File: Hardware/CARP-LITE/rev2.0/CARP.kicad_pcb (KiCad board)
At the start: 4 copper layers, 70.1 x 40 mm, 159 parts, among them J1 USB-C, J10 PYRO_2, J11 RF_L, J3 I2C1+3V3, J4 2/3S XT30, J5 UART+5V+I2C1, J6 PYRO_1, J7 SPI, J8 PWM1+5V1, J9 PWM2+5V1, Q5 SQ2318CES, Q6 SQ2318CES, Q7 SQ2318CES, SW1 SW_Push, SW2 SW_Push, U1 BQ25792, U10 TPS62130A, U2 W25Q128JVSIMTR (16MB), U3 BMP581, U4 RP2350_60QFN, U5 LSM6DSO, U7 TLV75733PDBV, U9 LR2021IMLTRT, Y1 ABM8-272-T3, Y2 ECS-TXO-25CSMV-320-AN-TR

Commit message: pcb and schematic changes
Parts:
- removed the REF** at (447.6, 301.7)
- moved J7 449.6 mm to (116.0, 77.0)
- moved L15 418.5 mm to (157.1, 81.3), turned to 90 degrees
- moved U1 374.6 mm to (160.8, 81.2), turned to 90 degrees
- moved C59 364.3 mm to (146.4, 64.5)
- moved L2 359.4 mm to (95.1, 82.3)
- moved FB1 358.2 mm to (99.1, 82.1)
- moved R37 357.1 mm to (152.3, 64.7)
- moved C26 351.6 mm to (161.7, 64.1)
- moved C61 350.5 mm to (155.0, 68.2)
- moved C58 349.9 mm to (151.7, 70.6)
- moved R36 349.7 mm to (154.4, 71.3)
- moved R23 349.7 mm to (156.8, 71.8)
- moved C35 348.5 mm to (144.3, 83.8)
- moved L8 348.3 mm to (110.9, 93.3)
- moved C1 348.3 mm to (120.8, 89.1)
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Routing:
- net +5V: track 95.3 -> 51.9 mm
- net /GPIO2: track 28.1 -> 13.4 mm
- net /GPIO3: track 27.5 -> 13.1 mm
- net /Radio/VR_PA: track 11.5 -> 0.00 mm, vias 2 -> 0
- net /GPIO8: track 16.8 -> 5.50 mm
- net /GPIO9: track 16.7 -> 5.96 mm
- net /Radio/RFI_LF: track 10.6 -> 0.00 mm
- net /GPIO20: track 31.3 -> 21.6 mm
- net /Radio/RFO_LF1: track 7.17 -> 0.00 mm
- net Net-(J11-In): track 7.16 -> 0.03 mm
- net Net-(U9-LXB): track 4.98 -> 0.00 mm
- net Net-(U10-FB): track 3.96 -> 0.00 mm
- net Net-(C46-Pad1): track 3.36 -> 0.01 mm
- net Net-(C48-Pad2): track 3.10 -> 0.10 mm
- net +3V3: track 26.9 -> 24.4 mm, vias 24 -> 21
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- removed copper zone on F.Cu, net +5V
- removed copper zone on F.Cu, net /BAT
- removed copper zone on F.Cu, net Net-(L14-Pad1)
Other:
- board text added: "SPI"
- board text removed: "L2"
- board text removed: "R23"

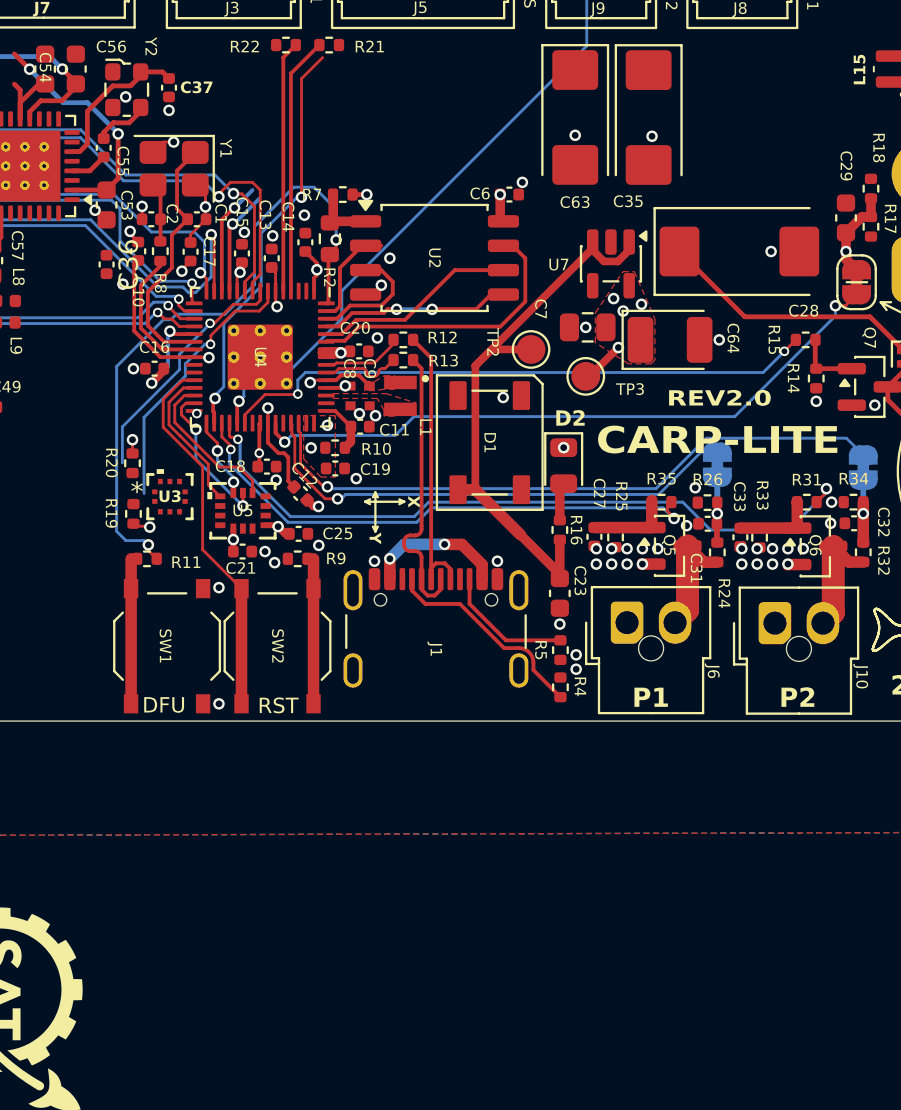
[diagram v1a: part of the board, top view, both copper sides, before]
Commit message: lithium charger is for carp lite rev 2, not carp dev
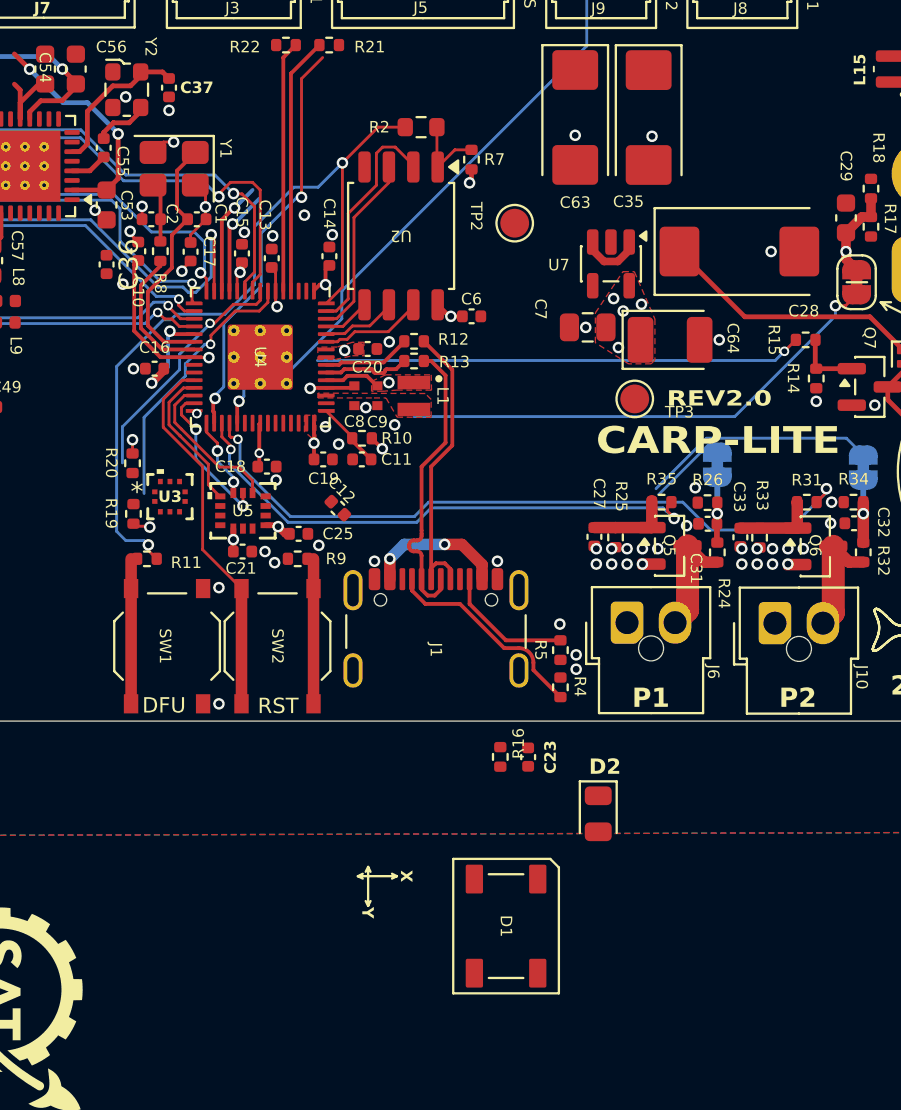
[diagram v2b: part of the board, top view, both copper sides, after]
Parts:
- C23: footprint Capacitor_SMD:C_0603_1608Metric -> Capacitor_SMD:C_0402_1005Metric
- moved D1 25.2 mm to (136.9, 125.9)
- moved D2 18.2 mm to (141.7, 120.0)
- moved R16 12.2 mm to (136.6, 117.1)
- moved C23 8.68 mm to (138.1, 117.1)
- moved R2 7.50 mm to (132.5, 84.3), turned to 0 degrees
- moved R7 6.94 mm to (135.1, 86.0), turned to 90 degrees
- moved C6 6.64 mm to (135.1, 94.2)
- moved TP2 6.63 mm to (137.3, 89.3)
- moved TP3 2.81 mm to (143.6, 98.5)
- moved C12 2.08 mm to (128.1, 104.1)
- moved U2 2.08 mm to (131.4, 90.0), turned to -90 degrees
- moved C11 1.71 mm to (129.4, 101.6), turned to 180 degrees
- moved R10 1.48 mm to (129.4, 100.5), turned to 180 degrees
- moved C14 1.45 mm to (127.7, 91.0)
- moved C19 0.79 mm to (127.4, 101.6)
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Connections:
- R18 pad 2: +2S -> /BAT
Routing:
- net +5V: track 51.9 -> 24.2 mm
- net Net-(U4-GPIO28_ADC2): track 26.1 -> 3.96 mm, vias 1 -> 0
- net Net-(U4-GPIO29_ADC3): track 33.4 -> 12.2 mm, vias 1 -> 0
- net /QSPI_SD3: track 14.9 -> 5.39 mm
- net Net-(U4-GPIO26_ADC0): track 34.4 -> 26.0 mm, vias 2 -> 1
- net /QSPI_SD0: track 10.0 -> 2.46 mm, vias 2 -> 0
- net /QSPI_SCLK: track 11.3 -> 3.95 mm
- net /QSPI_SS: track 34.3 -> 41.2 mm
- net /QSPI_SD1: track 5.44 -> 12.1 mm
- net /GPIO24: track 31.2 -> 25.4 mm, vias 2 -> 1
- net +1V1: track 18.7 -> 13.3 mm, vias 4 -> 3
- net /QSPI_SD2: track 6.44 -> 9.57 mm
- net Net-(D2-A): track 1.67 -> 0.00 mm
- net GND: track 7.36 -> 6.29 mm, vias 67 -> 63
- net /FLASH1_SS: track 3.55 -> 4.22 mm
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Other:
- board text removed: "R16"

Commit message: powersection
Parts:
- removed C72: 10u, Capacitor_SMD:C_0805_2012Metric
- C59, C69: footprint Capacitor_SMD:C_0603_1608Metric -> Capacitor_SMD:C_0402_1005Metric
- R36, R37: footprint Resistor_SMD:R_0603_1608Metric -> Resistor_SMD:R_0402_1005Metric
- moved C69 79.1 mm to (154.5, 82.1), turned to 90 degrees
- moved C65 78.9 mm to (150.6, 80.4), turned to 180 degrees
- moved R40 67.4 mm to (154.4, 76.4), turned to -90 degrees
- moved R38 67.0 mm to (152.8, 80.2), turned to -90 degrees
- moved C68 67.0 mm to (153.4, 76.4), turned to -90 degrees
- moved R28 65.6 mm to (153.8, 80.2), turned to 90 degrees
- moved R39 65.4 mm to (156.0, 75.9), turned to 180 degrees
- moved C34 60.9 mm to (155.8, 83.3), turned to -90 degrees
- moved C66 59.9 mm to (157.0, 84.7)
- moved C67 58.3 mm to (159.1, 84.7), turned to 180 degrees
- moved C5 56.8 mm to (159.4, 82.6), turned to -90 degrees
- moved C30 56.0 mm to (161.2, 80.1), turned to 180 degrees
- moved C28 51.7 mm to (195.9, 112.7)
- moved C76 48.7 mm to (152.2, 85.4), turned to 90 degrees
- moved C75 45.9 mm to (154.3, 85.4), turned to 90 degrees
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- renumbered TP2 to 5V
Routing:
- net +5V: track 24.2 -> 48.3 mm
- net /Lithium Charger/REGN: track 0.00 -> 13.3 mm, vias 0 -> 2
- net Net-(U1-BTST1): track 0.00 -> 8.20 mm, vias 0 -> 2
- net Net-(U1-BTST2): track 0.00 -> 7.32 mm, vias 0 -> 2
- net /GPIO8: track 5.50 -> 0.00 mm, vias 1 -> 0
- net Net-(U1-BATP): track 0.00 -> 5.26 mm
- net /GPIO26_ADC0: track 4.76 -> 1.18 mm
- net Net-(U10-FB): track 0.00 -> 2.95 mm
- net Net-(U1-TS): track 0.00 -> 2.77 mm
- net Net-(U1-SDRV): track 0.00 -> 2.53 mm
- net /CHRGR_OUT: track 0.00 -> 2.41 mm
- net /GPIO9: track 5.96 -> 3.71 mm, vias 1 -> 0
- net Net-(U1-PROG): track 0.00 -> 2.09 mm
- net Net-(U1-SW2): track 0.00 -> 2.05 mm
- net Net-(U1-SW1): track 0.00 -> 1.92 mm
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- added copper zone on F.Cu, net +5V
- added copper zone on F.Cu, net /BAT
- added copper zone on F.Cu, net /CHRGR_OUT
- added copper zone on F.Cu, net /VBUS
- added copper zone on F.Cu, net Net-(L14-Pad1)
- added copper zone on F.Cu, net Net-(U1-PMID)
- added copper zone on F.Cu, net Net-(U1-SW1)
- added copper zone on F.Cu, net Net-(U1-SW2)

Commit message: more rev2 changes
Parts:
- removed 5V, TP1: TestPoint, TestPoint:TestPoint_Pad_D1.5mm
- removed C29: 1u, Capacitor_SMD:C_0603_1608Metric
- removed R17: 100k, Resistor_SMD:R_0402_1005Metric
- removed R18: 200k, Resistor_SMD:R_0402_1005Metric
- removed R27, R29, R30: 0, Jumper:SolderJumper-2_P1.3mm_Bridged_RoundedPad1.0x1.5mm
- added C72: 1n, Capacitor_SMD:C_0402_1005Metric, F.Cu at (153.6, 88.9)
- added J12: PYRO_2_B, Connector_Molex:Molex_Nano-Fit_105313-xx02_1x02_P2.50mm_Horizontal, B.Cu at (153.4, 110.1)
- added J13: PYRO_1_B, Connector_Molex:Molex_Nano-Fit_105313-xx02_1x02_P2.50mm_Horizontal, B.Cu at (145.7, 110.1)
- added R42: 200k, Resistor_SMD:R_0402_1005Metric, F.Cu at (155.2, 88.4)
- added R43: 39k, Resistor_SMD:R_0402_1005Metric, F.Cu at (152.0, 88.4)
- added TP2: TestPoint, TestPoint:TestPoint_Pad_D1.5mm, F.Cu at (153.2, 94.3)
- R26, R34: value 100k -> 39k
- moved C22 113.5 mm to (90.8, 109.8)
- moved C24 113.5 mm to (91.3, 106.9)
- moved R41 70.6 mm to (151.6, 92.5)
- moved C28 59.1 mm to (140.6, 91.9), turned to 180 degrees
- moved C36 50.8 mm to (67.0, 78.3)
- moved U7 40.4 mm to (146.8, 96.0)
- moved C26 39.8 mm to (146.8, 92.0)
- moved C3 39.2 mm to (69.1, 73.2)
- moved C4 39.2 mm to (68.8, 74.6)
- moved C55 39.2 mm to (78.2, 74.8)
- moved C57 39.2 mm to (72.4, 80.6)
- moved FB2 39.2 mm to (70.0, 79.8)
- moved FB3 39.2 mm to (68.8, 76.2)
- moved U9 39.2 mm to (74.1, 75.7)
- moved Y2 39.2 mm to (79.4, 71.7)
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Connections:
- U4 pad 40: Net-(U4-GPIO26_ADC0) -> /GPIO26_ADC0
- U4 pad 42: Net-(U4-GPIO28_ADC2) -> /GPIO28_ADC2
- U4 pad 43: Net-(U4-GPIO29_ADC3) -> /GPIO29_ADC3
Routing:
- net +5V: track 48.3 -> 104.8 mm
- net /VBUS: track 7.37 -> 54.8 mm, vias 2 -> 3
- net /GPIO3: track 13.1 -> 55.3 mm, vias 0 -> 1
- net /GPIO2: track 13.4 -> 53.7 mm, vias 0 -> 1
- net /GPIO26_ADC0: track 1.18 -> 41.4 mm, vias 1 -> 2
- net /GPIO29_ADC3: track 3.85 -> 35.3 mm, vias 1 -> 2
- net /GPIO25: track 0.00 -> 27.6 mm, vias 0 -> 1
- net Net-(U4-GPIO26_ADC0): track 26.0 -> 0.00 mm, vias 1 -> 0
- net /GPIO28_ADC2: track 4.00 -> 27.7 mm, vias 1 -> 2
- net /GPIO6: track 24.2 -> 1.12 mm, vias 2 -> 1
- net /GPIO1: track 0.00 -> 19.4 mm, vias 0 -> 2
- net /GPIO10: track 19.7 -> 0.52 mm, vias 2 -> 1
- net /GPIO15: track 21.2 -> 2.22 mm, vias 2 -> 1
- net /GPIO20: track 21.6 -> 39.6 mm, vias 2 -> 1
- net /GPIO11: track 19.0 -> 1.35 mm, vias 2 -> 1
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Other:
- board text added: "2026.10"
- board text added: "CHRG"
- board text added: "PWR"
- board text removed: "2026.09"
- board text removed: "CUT IF V_IN ABV 10V"
- board text removed: "CUT TO ISOL ADC CONT. CHECK"
- board text removed: "P1 ADC"
- board text removed: "P2 ADC"
- board text removed: "R14"
- board text removed: "R15"

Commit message: rev pcb finished?
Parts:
- moved C36 50.4 mm to (116.0, 90.3), turned to 0 degrees
- moved FB2 44.0 mm to (114.0, 81.1), turned to 90 degrees
- moved Y2 41.6 mm to (118.9, 85.0)
- moved C51 41.2 mm to (114.7, 91.7), turned to 0 degrees
- moved C52 40.7 mm to (112.8, 91.7)
- moved C3 40.4 mm to (108.2, 83.3)
- moved C4 40.2 mm to (107.7, 84.7)
- moved FB3 40.1 mm to (107.7, 86.2)
- moved C55 40.1 mm to (116.8, 85.8)
- moved U9 40.1 mm to (112.8, 86.0)
- moved L13 39.4 mm to (114.2, 90.2), turned to -90 degrees
- moved C22 38.4 mm to (121.7, 87.0), turned to -90 degrees
- moved C24 37.6 mm to (121.7, 84.8), turned to 90 degrees
- moved C57 36.9 mm to (108.3, 89.3), turned to 180 degrees
- moved C50 35.7 mm to (107.0, 96.9), turned to 0 degrees
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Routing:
- net /GPIO14: track 2.69 -> 37.3 mm, vias 1 -> 2
- net /GPIO15: track 2.22 -> 31.9 mm, vias 1 -> 2
- net /GPIO12: track 1.15 -> 26.3 mm, vias 1 -> 2
- net /GPIO9: track 0.00 -> 21.7 mm, vias 0 -> 1
- net /GPIO8: track 0.00 -> 20.9 mm, vias 0 -> 1
- net /GPIO6: track 1.12 -> 21.0 mm, vias 1 -> 2
- net /GPIO13: track 2.08 -> 18.7 mm, vias 1 -> 2
- net /GPIO11: track 1.35 -> 16.4 mm, vias 1 -> 2
- net /GPIO10: track 0.52 -> 14.5 mm, vias 1 -> 2
- net Net-(U9-VPAX1): track 0.15 -> 12.4 mm, vias 0 -> 2
- net Net-(U9-VDCC2): track 3.49 -> 15.6 mm, vias 0 -> 2
- net /Radio/VR_PA: track 0.00 -> 11.3 mm, vias 0 -> 2
- net Net-(J11-In): track 0.03 -> 11.3 mm
- net +3V3: track 22.1 -> 33.1 mm, vias 21 -> 26
- net /GPIO0: track 0.00 -> 9.77 mm, vias 0 -> 2
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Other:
- board text added: "3S (12.6V) MAX DSGN 2S (8.4V)"
- board text removed: "UHF"
- board text removed: "≥ 10V CUT ADC IF NOT EXPLOD 17V MAX DSGN 8.4V"

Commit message: move around silkscreen
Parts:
- moved R4 1.87 mm to (139.4, 111.6)
- moved R5 1.87 mm to (139.4, 109.7)
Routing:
- net Net-(J1-CC1): track 10.9 -> 9.61 mm
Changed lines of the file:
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@@
 		)
 		(fp_text user "${REFERENCE}"
-			(at -1.81 0 0)
+			(at -1.9 0 0)
 			(unlocked yes)
 			(layer "F.SilkS")
@@
 	(footprint "Resistor_SMD:R_0402_1005Metric"
 		(layer "F.Cu")
-		(at 139.73 111.53 -90)
+		(at 139.4 109.69 -90)
 		(descr "Resistor SMD 0402 (1005 Metric), square (rectangular) end terminal, IPC-7351 nominal, (Body size source: IPC-SM-782 page 72, https://www.pcb-3d.com/wordpress/wp-content/uploads/ipc-sm-782a_amendment_1_and_2.pdf)")
 		(tags "resistor")
 		(property "Reference" "R5"
-			(at -0.005 0.93 270)
+			(at -0.005 -0.9 270)
 			(unlocked yes)
 			(layer "F.SilkS")
@@
 		(tags "RC Connector XT30")
 		(property "Reference" "J4"
-			(at -2.5 -2.413 90)
+			(at -2.5 -2.413 270)
+			(unlocked yes)
 			(layer "F.SilkS")
 			(effects
@@
 	(footprint "Resistor_SMD:R_0402_1005Metric"
 		(layer "F.Cu")
-		(at 139.73 113.465 90)
+		(at 139.4 111.625 90)
 		(descr "Resistor SMD 0402 (1005 Metric), square (rectangular) end terminal, IPC-7351 nominal, (Body size source: IPC-SM-782 page 72, https://www.pcb-3d.com/wordpress/wp-content/uploads/ipc-sm-782a_amendment_1_and_2.pdf)")
 		(tags "resistor")
 		(property "Reference" "R4"
-			(at 0.04 -0.93 270)
+			(at 0.025 0.9 270)
 			(unlocked yes)
 			(layer "F.SilkS")
@@
 		)
 		(fp_text user "${REFERENCE}"
-			(at 1.365 0 0)
+			(at 1.365 -0.2 0)
 			(unlocked yes)
 			(layer "F.SilkS")
@@
 		)
 		(fp_text user "${REFERENCE}"
-			(at -1.81 0 0)
+			(at -1.91 0 0)
 			(unlocked yes)
 			(layer "F.SilkS")
@@
 		)
 		(fp_text user "${REFERENCE}"
-			(at 2.3811 -0.149999 0)
+			(at 2.4811 -0.149999 0)
 			(unlocked yes)
 			(layer "F.SilkS")
@@
 		)
 		(fp_text user "${REFERENCE}"
-			(at 1.34 0 0)
+			(at 1.34 0.1 0)
 			(unlocked yes)
 			(layer "F.SilkS")
@@
 	)
 	(via
-		(at 140.55 112.525)
+		(at 140.3 110.7)
 		(size 0.6)
 		(drill 0.35)
@@
 	)
 	(segment
-		(start 135 109.125)
-		(end 136.895 111.02)
+		(start 138.05 110.35)
+		(end 139.22 109.18)
+		(width 0.2)
+		(layer "F.Cu")
+		(net "Net-(J1-CC2)")
+	)
+	(segment
+		(start 135 109.130026)
+		(end 136.219974 110.35)
 		(width 0.2)
 		(layer "F.Cu")
@@
 	(segment
 		(start 135 107.835)
-		(end 135 109.125)
+		(end 135 109.130026)
 		(width 0.2)
 		(layer "F.Cu")
@@
 	)
 	(segment
-		(start 136.895 111.02)
-		(end 139.73 111.02)
+		(start 136.219974 110.35)
+		(end 138.05 110.35)
+		(width 0.2)
+		(layer "F.Cu")
+		(net "Net-(J1-CC2)")
+	)
+	(segment
+		(start 139.22 109.18)
+		(end 139.4 109.18)
 		(width 0.2)
 		(layer "F.Cu")
@@
 	)
 	(segment
-		(start 136.8 111.425)
-		(end 134.5 109.125)
-		(width 0.2)
-		(layer "F.Cu")
-		(net "Net-(J1-CC1)")
-	)
-	(segment
-		(start 138.325 112.57)
-		(end 138.325 112.182058)
+		(start 132 107.835)
+		(end 132 108.425)
 		(width 0.2)
 		(layer "F.Cu")
@@
 	)
 	(segment
-		(start 134.5 109.125)
-		(end 132.7 109.125)
+		(start 132.7 109.125)
+		(end 134.5 109.125)
 		(width 0.2)
 		(layer "F.Cu")
@@
 	)
 	(segment
-		(start 139.73 113.975)
-		(end 138.325 112.57)
+		(start 136.075 110.7)
+		(end 138.1 110.7)
 		(width 0.2)
 		(layer "F.Cu")
@@
 	)
 	(segment
-		(start 132.7 109.125)
-		(end 132 108.425)
+		(start 139.4 112)
+		(end 139.4 112.135)
 		(width 0.2)
 		(layer "F.Cu")
@@
 	)
 	(segment
-		(start 137.567942 111.425)
-		(end 136.8 111.425)
+		(start 138.1 110.7)
+		(end 139.4 112)
 		(width 0.2)
 		(layer "F.Cu")
@@
 	(segment
 		(start 132 108.425)
-		(end 132 107.835)
+		(end 132.7 109.125)
 		(width 0.2)
 		(layer "F.Cu")
 		(net "Net-(J1-CC1)")
 	)
-	(arc
-		(start 137.567942 111.425)
-		(mid 138.103263 111.646737)
-		(end 138.325 112.182058)
+	(segment
+		(start 134.5 109.125)
+		(end 136.075 110.7)
 		(width 0.2)
 		(layer "F.Cu")
